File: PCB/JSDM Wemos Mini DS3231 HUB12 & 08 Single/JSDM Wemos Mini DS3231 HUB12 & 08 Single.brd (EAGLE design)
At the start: 14 parts, among them X1 PSU

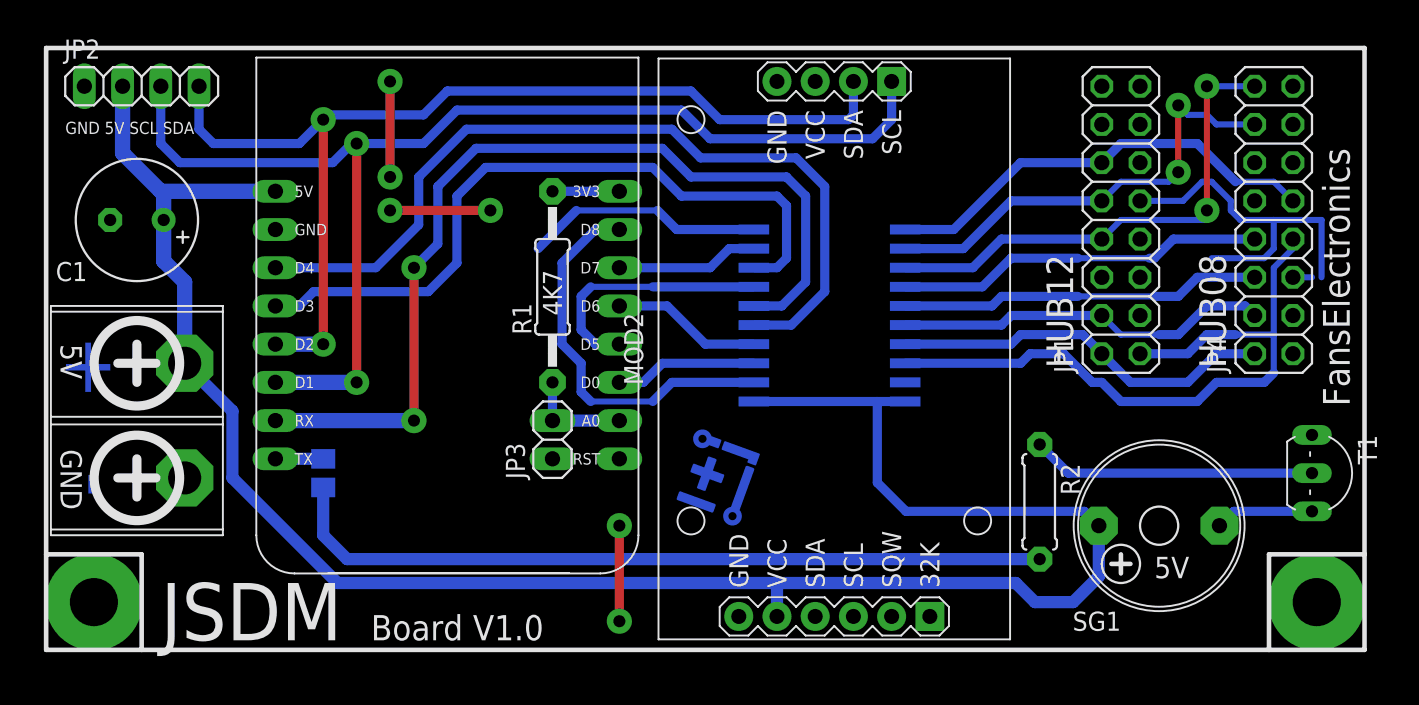
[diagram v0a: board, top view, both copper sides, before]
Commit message: JSDM PCB Single Layer ESP8266 + ESP32
Desain PCB SIngle Layer versi:
- Wemos D1 mini HUB12 + HUB08
- Wemos D1 Mini 3x HUB12
- ESP32 Devkit HUB12 + HUB08
- ESP32 Devkit Mini 3x HUB12
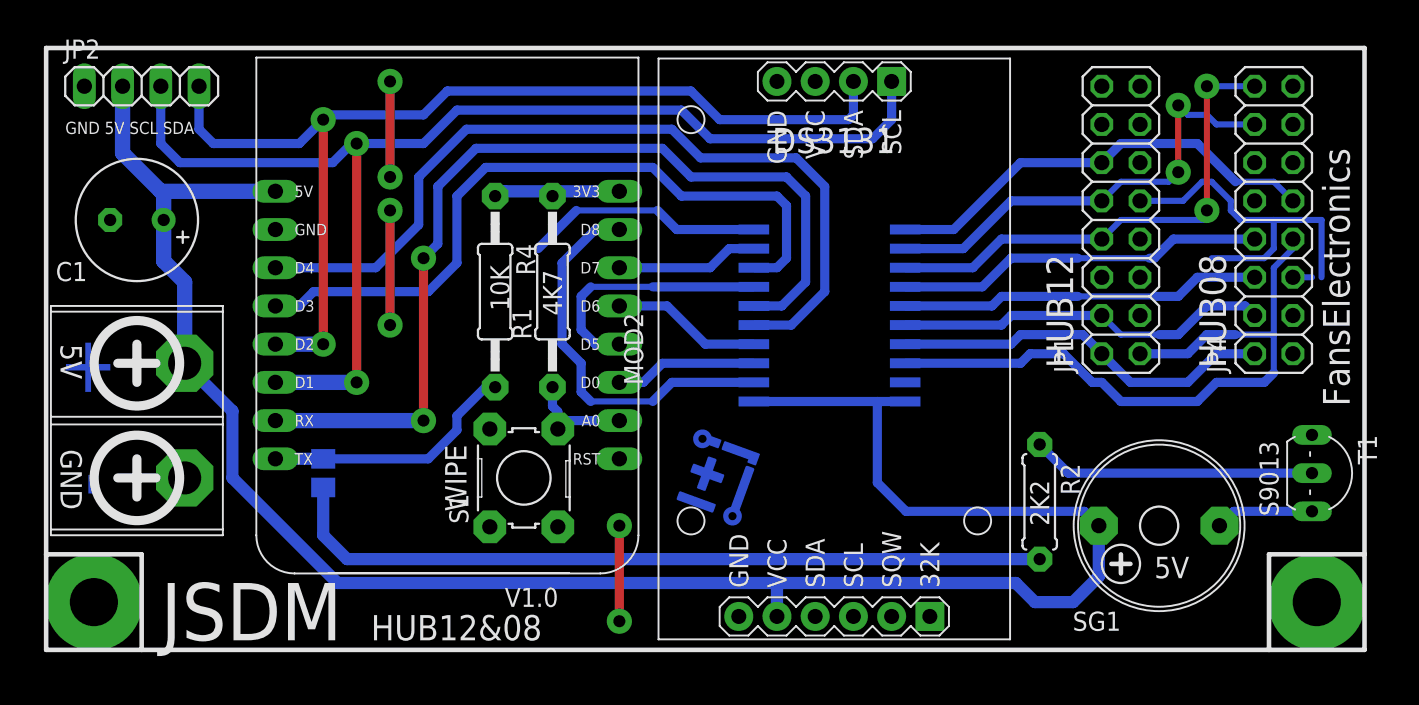
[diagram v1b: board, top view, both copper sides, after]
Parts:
- removed JP3: (no value), FansElectronics-Header:1X02
- added R4: 10K, FansElectronics-RCL:0207/12
- added S1: WIPE, FansElectronics-Switch:TACT-6X6MM-OCTAGON
- R1: value 10K -> 4K7
- moved R1 0.32 mm to (59.1, 48.6)
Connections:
- removed net N$1: R1.2, WEMOS1.3V3
- removed net WIPING: JP3.2, R1.1, WEMOS1.A0
- new net +3V3: R1.2, R4.1, WEMOS1.3V3
- new net WIPE: R1.1, S1.4, WEMOS1.A0
- net GND: now also S1.1, S1.2; no longer JP3.1
- net TX: now also R4.2
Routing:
- net TX: track 3.18 -> 17.1 mm
- net +3V3: track 0.00 -> 11.6 mm
- net WIPE: track 0.00 -> 7.25 mm
- net WIPING: track 6.98 -> 0.00 mm
- net N$1: track 4.45 -> 0.00 mm
- net GND: track 60.7 -> 61.6 mm
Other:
- board text added: "10K"
- board text added: "2K2"
- board text added: "DS3131"
- board text added: "HUB12&08"
- board text added: "S9013"
- board text added: "V1.0"
- board text added: "WIPE"
- board text removed: "Board V1.0"
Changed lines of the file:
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@@
 <layer number="17" name="Pads" color="2" fill="1" visible="yes" active="yes"/>
 <layer number="18" name="Vias" color="2" fill="1" visible="yes" active="yes"/>
-<layer number="19" name="Unrouted" color="6" fill="1" visible="yes" active="yes"/>
+<layer number="19" name="Unrouted" color="6" fill="1" visible="no" active="yes"/>
 <layer number="20" name="Dimension" color="15" fill="1" visible="no" active="yes"/>
 <layer number="21" name="tPlace" color="7" fill="1" visible="yes" active="yes"/>
@@
 <text x="59.69" y="46.99" size="1.27" layer="21" font="vector" ratio="15" rot="R90">4K7</text>
 <text x="33.02" y="25.4" size="3.81" layer="21" font="vector" ratio="20">JSDM</text>
-<text x="46.99" y="25.4" size="1.6764" layer="21" font="vector" ratio="15">Board V1.0</text>
+<text x="46.99" y="25.4" size="1.6764" layer="21" font="vector" ratio="15">HUB12&amp;08</text>
 <wire x1="25.4" y1="64.77" x2="113.03" y2="64.77" width="0.3048" layer="21"/>
 <wire x1="113.03" y1="64.77" x2="113.03" y2="31.115" width="0.3048" layer="21"/>
@@
 <wire x1="113.03" y1="31.115" x2="106.68" y2="31.115" width="0.3048" layer="21"/>
 <wire x1="106.68" y1="31.115" x2="106.68" y2="24.765" width="0.3048" layer="21"/>
+<text x="55.88" y="27.6225" size="1.27" layer="21" font="vector" ratio="15" rot="SR0">V1.0</text>
+<text x="56.1975" y="47.3075" size="1.27" layer="21" font="vector" ratio="15" rot="R90">10K</text>
+<text x="53.34" y="33.9725" size="1.4224" layer="21" font="vector" ratio="20" rot="SR90">WIPE</text>
+<text x="92.075" y="33.02" size="1.27" layer="21" font="vector" ratio="15" rot="SR90">2K2</text>
+<text x="107.315" y="33.655" size="1.27" layer="21" font="vector" ratio="15" rot="SR90">S9013</text>
+<text x="73.66" y="57.785" size="1.6764" layer="21" font="vector" ratio="15" rot="SR0">DS3131</text>
 </plain>
 <attributes>
@@
 <element name="JP1" library="FansElectronics-Header" package="2X08" value="HUB12" x="96.8375" y="53.34" rot="R90"/>
 <element name="JP2" library="FansElectronics-Header" package="1X04" value="I2C" x="31.75" y="62.23"/>
-<element name="JP3" library="FansElectronics-Header" package="1X02" value="" x="59.055" y="38.735" rot="R90"/>
 <element name="JP4" library="FansElectronics-Header" package="2X08" value="HUB08" x="106.9975" y="53.34" rot="R90"/>
 <element name="MOD2" library="FansElectronics-Modul" package="RTC-DS3231-MIRROR" value="RTC-3231MIRROR" x="77.7875" y="44.7675" rot="R90"/>
-<element name="R1" library="FansElectronics-RCL" package="0207/12" value="10K" x="59.055" y="48.895" rot="R90"/>
+<element name="R1" library="FansElectronics-RCL" package="0207/12" value="4K7" x="59.055" y="48.5775" rot="R90"/>
 <element name="R2" library="FansElectronics-RCL" package="0207/7" value="2K2" x="91.44" y="34.6075" rot="R270"/>
 <element name="SG1" library="FansElectronics-Buzzer" package="5V" value="5V-PCB" x="99.3775" y="33.02" rot="R180"/>
@@
 <element name="X1" library="FansElectronics-Con-Screw" package="TB2" value="PSU" x="34.6075" y="40.005" rot="R270"/>
 <element name="R3" library="FansElectronics-RCL" package="M0805" value="PROG" x="43.815" y="36.5125" rot="MR270"/>
+<element name="S1" library="FansElectronics-Switch" package="TACT-6X6MM-OCTAGON" value="WIPE" x="57.15" y="36.195" rot="R90"/>
+<element name="R4" library="FansElectronics-RCL" package="0207/12" value="10K" x="55.245" y="48.5775" rot="R270"/>
 </elements>
 <signals>
@@
 <contactref element="MOD2" pad="J2.4"/>
 <contactref element="JP2" pad="1"/>
-<contactref element="JP3" pad="1"/>
 <contactref element="JP4" pad="15"/>
 <contactref element="JP4" pad="1"/>
@@
 <via x="48.26" y="56.1975" extent="1-16" drill="0.8" diameter="1.6764" shape="octagon"/>
 <via x="48.26" y="53.975" extent="1-16" drill="0.8" diameter="1.6764" shape="octagon"/>
-<via x="54.9275" y="53.975" extent="1-16" drill="0.8" diameter="1.6764" shape="octagon"/>
+<via x="48.26" y="46.355" extent="1-16" drill="0.8" diameter="1.6764" shape="octagon"/>
 <via x="48.26" y="62.5475" extent="1-16" drill="0.8" diameter="1.6764" shape="octagon"/>
 <wire x1="48.26" y1="62.5475" x2="48.26" y2="56.1975" width="0.6096" layer="1"/>
-<wire x1="48.26" y1="53.975" x2="54.9275" y2="53.975" width="0.6096" layer="1"/>
+<wire x1="48.26" y1="53.975" x2="48.26" y2="46.355" width="0.6096" layer="1"/>
 <wire x1="102.87" y1="50.8" x2="106.3625" y2="50.8" width="0.4064" layer="16"/>
 <wire x1="106.3625" y1="50.8" x2="106.9975" y2="51.435" width="0.4064" layer="16"/>
 <wire x1="106.9975" y1="51.435" x2="106.9975" y2="53.34" width="0.4064" layer="16"/>
+<contactref element="S1" pad="1"/>
+<contactref element="S1" pad="2"/>
 </signal>
 <signal name="D3">
@@
 <wire x1="86.995" y1="50.165" x2="82.4992" y2="50.165" width="0.6096" layer="16"/>
 </signal>
-<signal name="N$1">
-<contactref element="WEMOS1" pad="3V3"/>
-<contactref element="R1" pad="2"/>
-<wire x1="59.055" y1="55.245" x2="63.5" y2="55.245" width="0.6096" layer="16"/>
-</signal>
 <signal name="C">
 <contactref element="JP4" pad="6"/>
@@
 <wire x1="53.975" y1="58.1025" x2="51.435" y2="55.5625" width="0.6096" layer="16"/>
 <wire x1="51.435" y1="55.5625" x2="51.435" y2="51.7525" width="0.6096" layer="16"/>
-<wire x1="51.435" y1="51.7525" x2="49.8475" y2="50.165" width="0.6096" layer="16"/>
-<via x="49.8475" y="50.165" extent="1-16" drill="0.8" diameter="1.6764" shape="octagon"/>
-<wire x1="49.8475" y1="50.165" x2="49.8475" y2="40.005" width="0.6096" layer="1"/>
-<via x="49.8475" y="40.005" extent="1-16" drill="0.8" diameter="1.6764" shape="octagon"/>
-<wire x1="49.8475" y1="40.005" x2="40.64" y2="40.005" width="1.016" layer="16"/>
+<wire x1="51.435" y1="51.7525" x2="50.4825" y2="50.8" width="0.6096" layer="16"/>
+<via x="50.4825" y="50.8" extent="1-16" drill="0.8" diameter="1.6764" shape="octagon"/>
+<wire x1="50.4825" y1="50.8" x2="50.4825" y2="40.005" width="0.6096" layer="1"/>
+<via x="50.4825" y="40.005" extent="1-16" drill="0.8" diameter="1.6764" shape="octagon"/>
+<wire x1="50.4825" y1="40.005" x2="40.64" y2="40.005" width="1.016" layer="16"/>
 </signal>
 <signal name="TX">
@@
 <wire x1="40.64" y1="37.465" x2="43.815" y2="37.465" width="0.8128" layer="16"/>
 <wire x1="43.815" y1="37.465" x2="43.815" y2="37.4625" width="0.8128" layer="16"/>
+<contactref element="R4" pad="2"/>
+<wire x1="43.815" y1="37.4625" x2="50.7975" y2="37.4625" width="0.6096" layer="16"/>
+<wire x1="50.7975" y1="37.4625" x2="52.705" y2="39.37" width="0.6096" layer="16"/>
+<wire x1="52.705" y1="39.37" x2="52.705" y2="40.3225" width="0.6096" layer="16"/>
+<wire x1="52.705" y1="40.3225" x2="54.61" y2="42.2275" width="0.6096" layer="16"/>
+<wire x1="54.61" y1="42.2275" x2="55.245" y2="42.2275" width="0.6096" layer="16"/>
 </signal>
 <signal name="N$2">
@@
 <wire x1="45.4025" y1="30.7975" x2="91.44" y2="30.7975" width="0.8128" layer="16"/>
 </signal>
-<signal name="WIPING">
-<contactref element="JP3" pad="2"/>
-<contactref element="R1" pad="1"/>
-<wire x1="59.055" y1="42.545" x2="59.055" y2="40.005" width="0.6096" layer="16"/>
+<signal name="WIPE">
 <contactref element="WEMOS1" pad="A0"/>
-<wire x1="59.055" y1="40.005" x2="63.5" y2="40.005" width="0.8128" layer="16"/>
+<contactref element="R1" pad="1"/>
+<contactref element="S1" pad="4"/>
+<wire x1="63.5" y1="40.005" x2="59.9694" y2="40.005" width="0.6096" layer="16"/>
+<wire x1="59.9694" y1="40.005" x2="59.4106" y2="39.4462" width="0.6096" layer="16"/>
+<wire x1="59.4106" y1="39.4462" x2="59.4106" y2="40.6019" width="0.6096" layer="16"/>
+<wire x1="59.4106" y1="40.6019" x2="59.055" y2="40.9575" width="0.6096" layer="16"/>
+<wire x1="59.055" y1="40.9575" x2="59.055" y2="42.2275" width="0.6096" layer="16"/>
+</signal>
+<signal name="+3V3">
+<contactref element="WEMOS1" pad="3V3"/>
+<contactref element="R4" pad="1"/>
+<wire x1="63.5" y1="55.245" x2="55.88" y2="55.245" width="0.8128" layer="16"/>
+<wire x1="55.88" y1="55.245" x2="55.245" y2="54.9275" width="0.8128" layer="16"/>
+<contactref element="R1" pad="2"/>
+<wire x1="55.88" y1="55.245" x2="58.7375" y2="55.245" width="0.6096" layer="16"/>
+<wire x1="58.7375" y1="55.245" x2="59.055" y2="54.9275" width="0.6096" layer="16"/>
 </signal>
 </signals>
